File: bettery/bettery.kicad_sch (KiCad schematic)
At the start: 77 parts, among them Q1 WMB014N06LG4, Q2 WMB014N06LG4, Q3 SL2319A, Q4 MMBT3904, SW1 SW_Push, U1 L9961

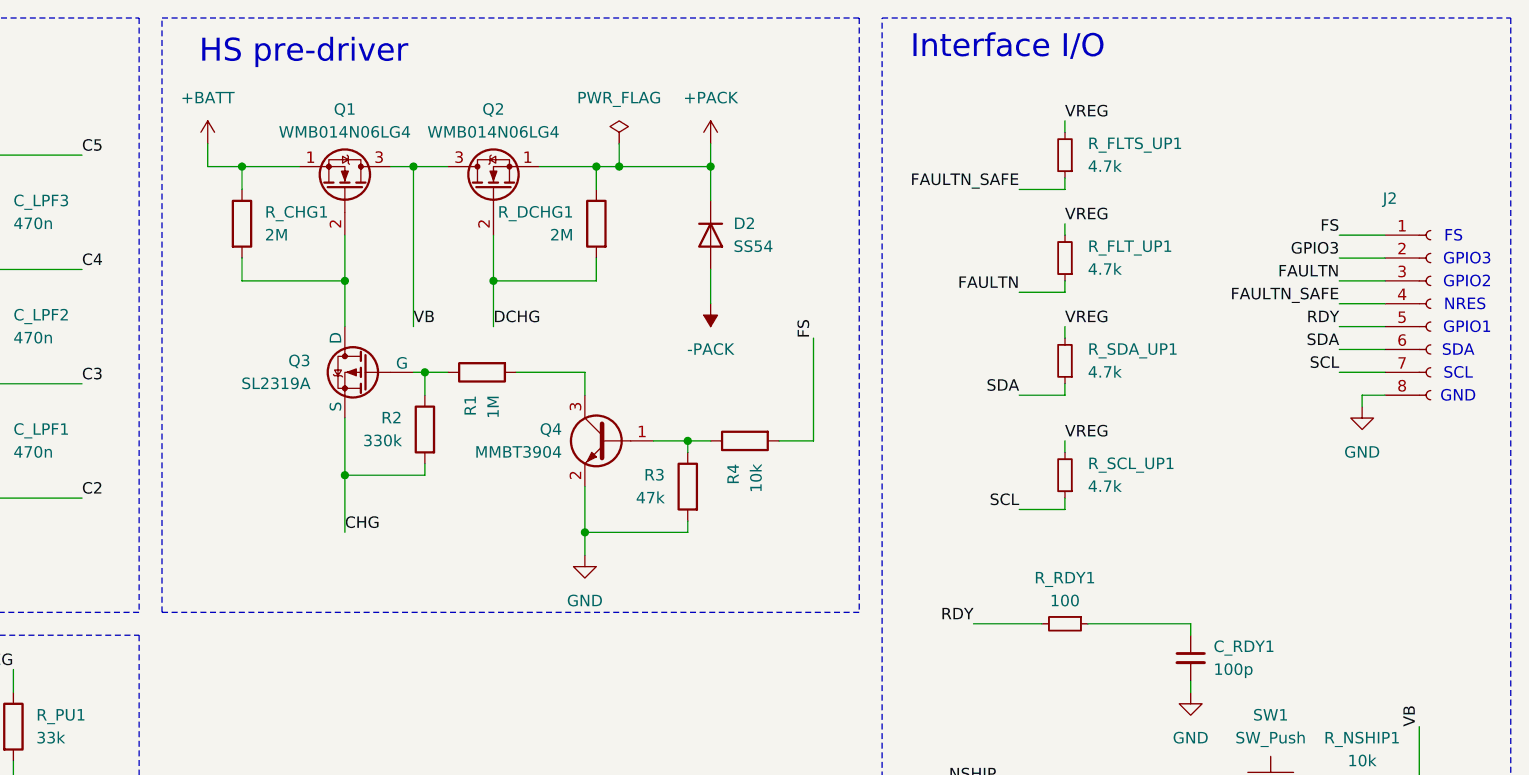
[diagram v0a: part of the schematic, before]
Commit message: remove fail-safe switch
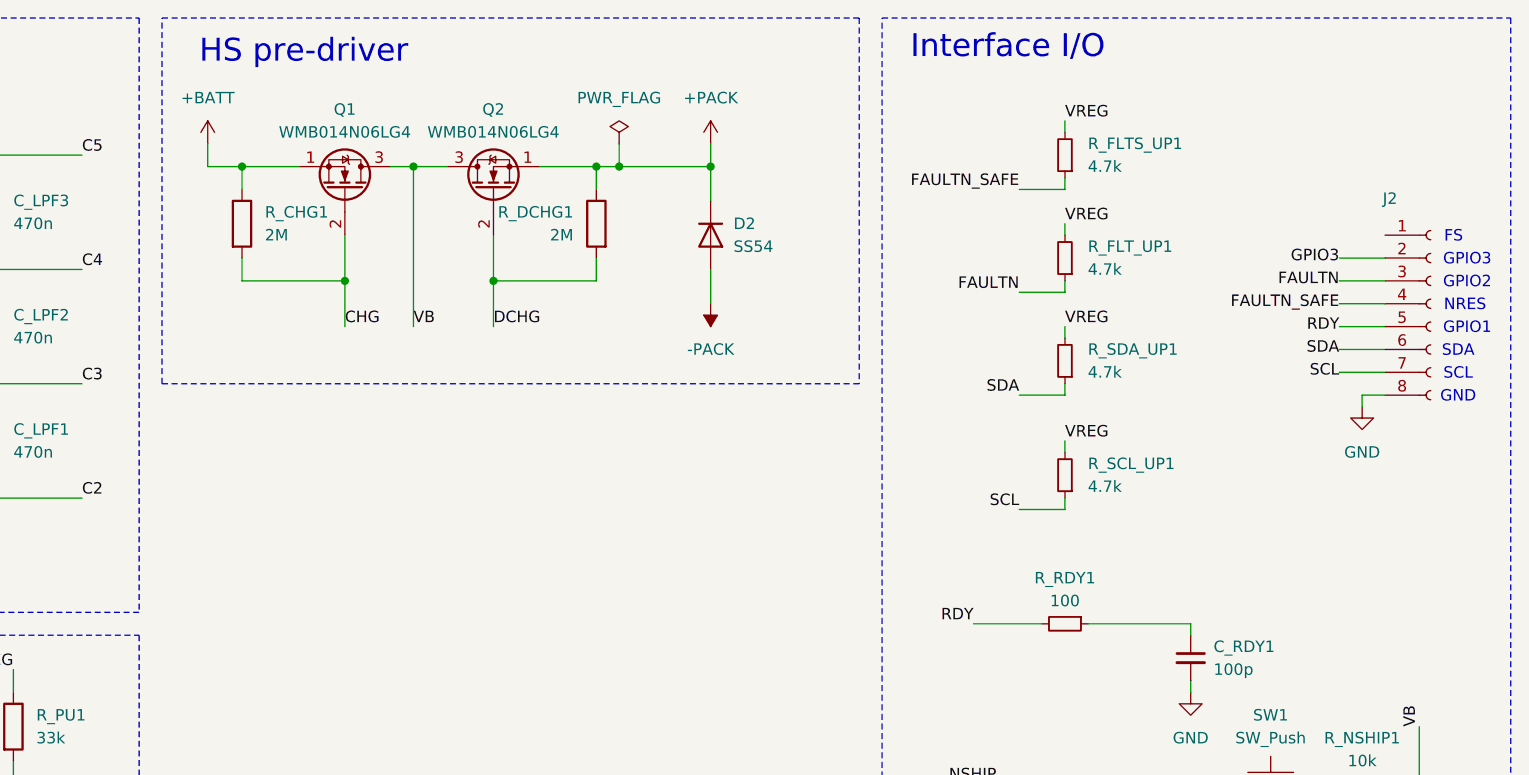
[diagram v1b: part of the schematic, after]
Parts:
- removed Q3: SL2319A, Package_TO_SOT_SMD:SOT-23_Handsoldering, symbol Simulation_SPICE:PMOS
- removed Q4: MMBT3904, Package_TO_SOT_SMD:SOT-23_Handsoldering, symbol Transistor_BJT:Q_NPN_BEC
- removed R1: 1M, Resistor_SMD:R_0603_1608Metric_Pad0.98x0.95mm_HandSolder, symbol Device:R
- removed R2: 330k, Resistor_SMD:R_0603_1608Metric_Pad0.98x0.95mm_HandSolder, symbol Device:R
- removed R3: 47k, Resistor_SMD:R_0603_1608Metric_Pad0.98x0.95mm_HandSolder, symbol Device:R
- removed R4: 10k, Resistor_SMD:R_0603_1608Metric_Pad0.98x0.95mm_HandSolder, symbol Device:R
- J_CHG1: footprint (none) -> Connector_BarrelJack:BarrelJack_GCT_DCJ200-10-A_Horizontal; Link (none) -> https://www.digikey.com/en/products/detail/tensility-intern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
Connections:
- net CHG: now also Q1.2 (G), R_CHG1.2
- net FS: no longer names the net of J2.1 (Pin_1)

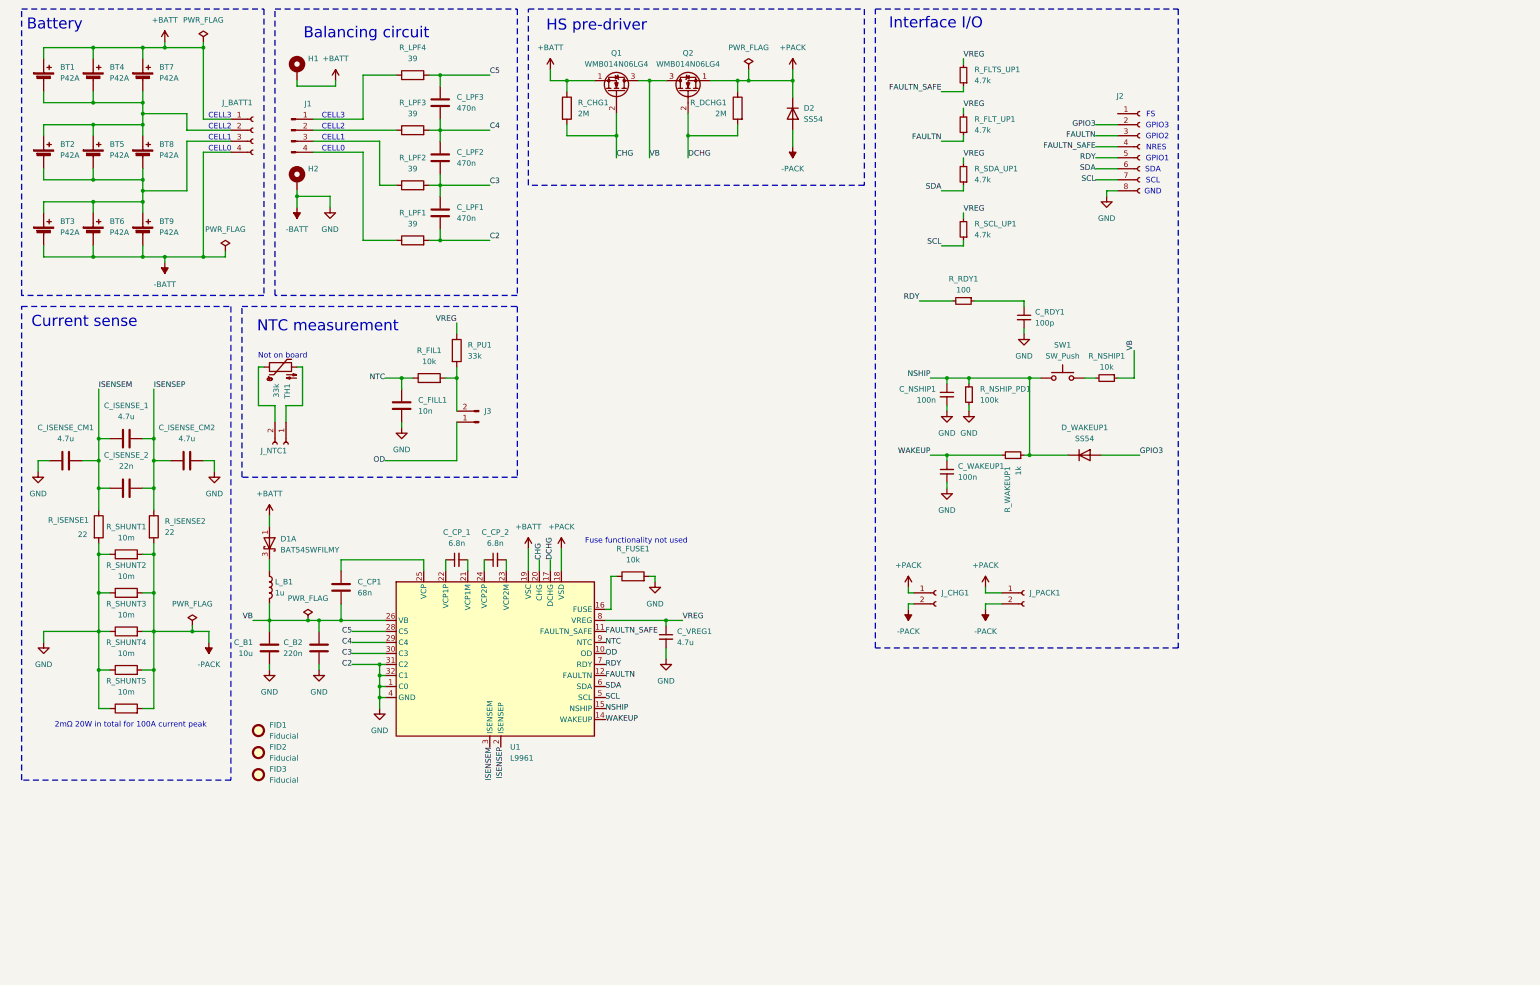
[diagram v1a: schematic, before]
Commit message: add mcu
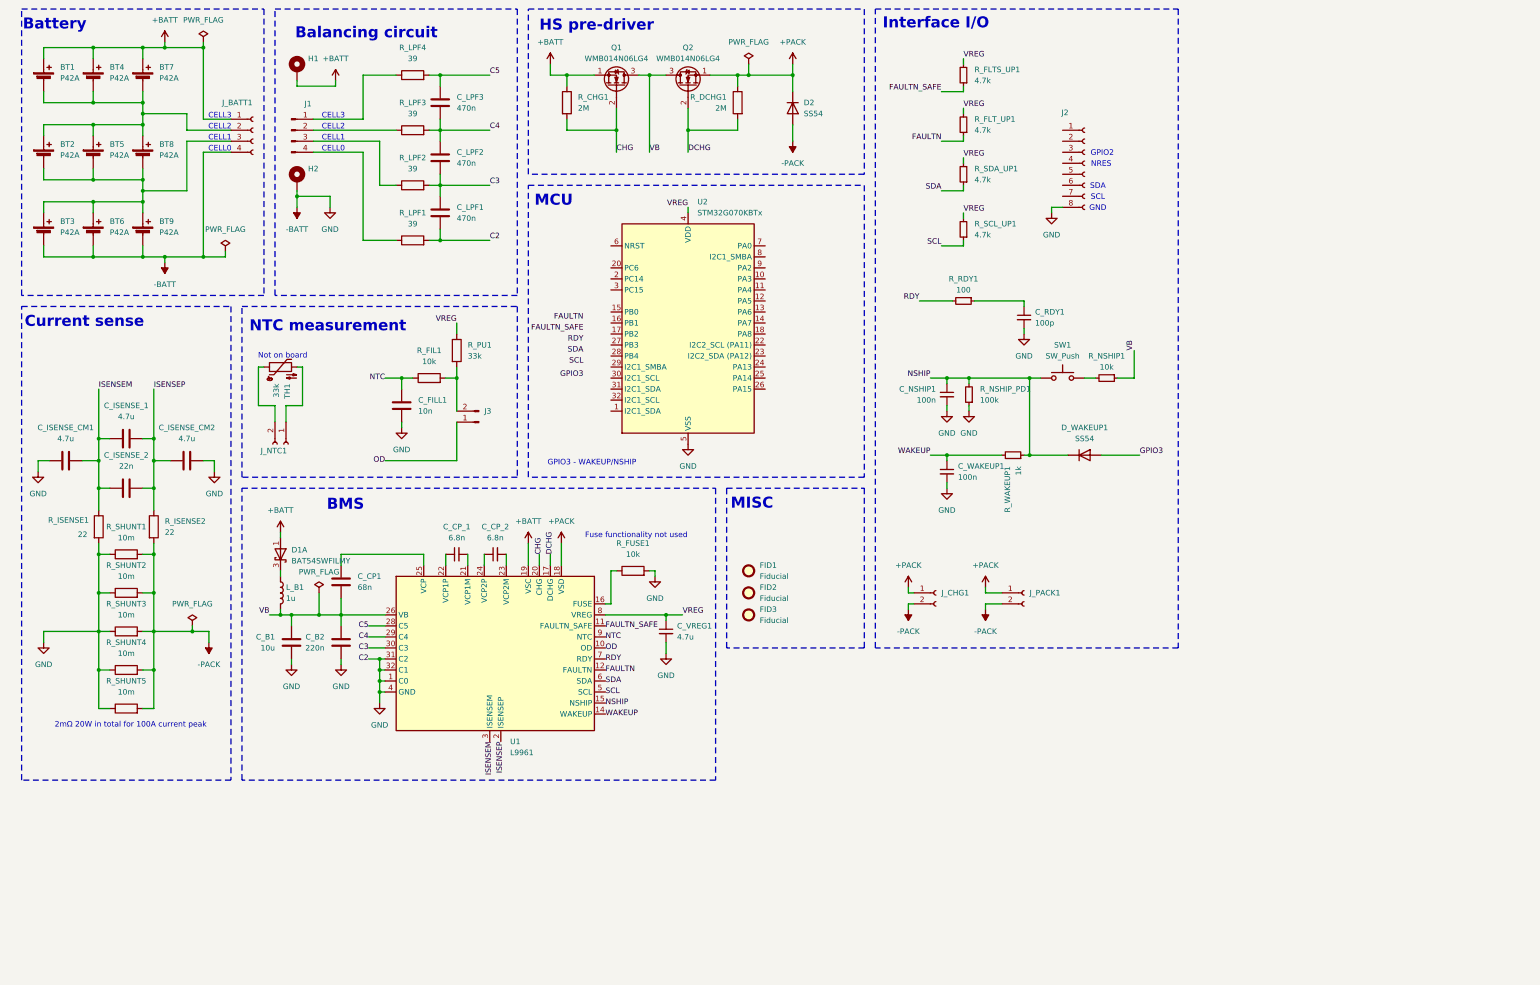
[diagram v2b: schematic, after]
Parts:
- added U2: STM32G070KBTx, Package_QFP:LQFP-32_7x7mm_P0.8mm, symbol MCU_ST_STM32G0:STM32G070KBTx
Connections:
- net -BATT: now also U2.5 (VSS)
- net FAULTN: no longer J2.3 (Pin_3)
- net FAULTN_SAFE: no longer J2.4 (Pin_4)
- net GPIO3: no longer J2.2 (Pin_2)
- net RDY: no longer J2.5 (Pin_5)
- net SCL: no longer J2.7 (Pin_7)
- net SDA: no longer J2.6 (Pin_6)
- net VREG: now also U2.4 (VDD)
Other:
- note added: "BMS"
- note added: "GPIO3 - WAKEUP/NSHIP"
- note added: "MCU"
- note added: "MISC"
- note removed: "FS"
- note removed: "GPIO1"
- note removed: "GPIO3"
- moved on the sheet: C_B1, C_B2, C_CP1, C_CP_1, C_CP_2, C_VREG1, D1A, D2, FID1, FID2, FID3, J2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

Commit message: complete routing
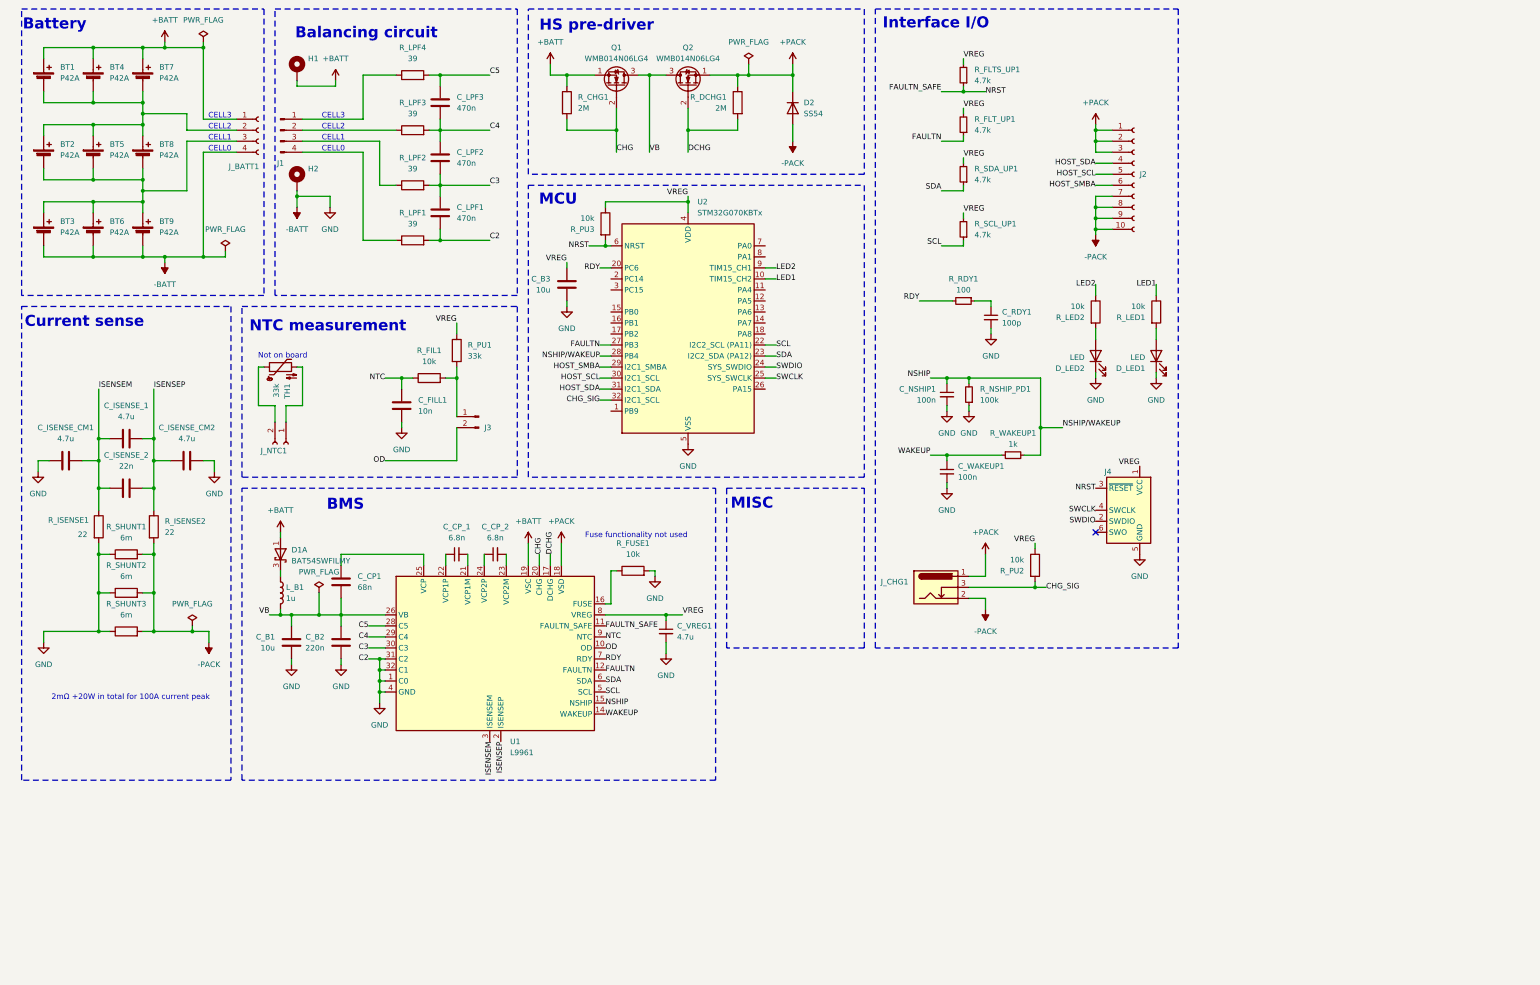
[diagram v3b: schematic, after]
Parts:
- removed D_WAKEUP1: SS54, Diode_SMD:D_SMA_Handsoldering, symbol Device:D
- removed FID1, FID2, FID3: Fiducial, Fiducial:Fiducial_1mm_Mask3mm, symbol Mechanical:Fiducial
- removed J2: ~, Connector_JST:JST_PH_B8B-PH-K_1x08_P2.00mm_Vertical, symbol Connector:Conn_01x08_Socket
- removed J_CHG1: ~, Connector_BarrelJack:BarrelJack_GCT_DCJ200-10-A_Horizontal, symbol Connector:Conn_01x02_Socket
- removed J_PACK1: ~, symbol Connector:Conn_01x02_Socket
- removed R_NSHIP1: 10k, Resistor_SMD:R_0603_1608Metric_Pad0.98x0.95mm_HandSolder, symbol Device:R_Small
- removed R_SHUNT4, R_SHUNT5: 10m, Resistor_SMD:R_2816_7142Metric_Pad3.20x4.45mm_HandSolder, symbol Device:R
- removed SW1: SW_Push, Button_Switch_THT:SW_PUSH_6mm, symbol Switch:SW_Push
- added C_B3: 10u, Capacitor_SMD:C_0603_1608Metric, symbol Device:C
- added D_LED1, D_LED2: LED, LED_SMD:LED_0603_1608Metric, symbol Device:LED
- added J2: Conn_01x10_Socket, bettery:1674231_SMD, symbol Connector:Conn_01x10_Socket
- added J4: Conn_ARM_SWD_TagConnect_TC2030, bettery:WR-WST-REDFIT-IDC-6pin, symbol Connector:Conn_ARM_SWD_TagConnect_TC2030
- added J_CHG1: Barrel_Jack_Switch, Connector_BarrelJack:BarrelJack_GCT_DCJ200-10-A_Horizontal, symbol Connector:Barrel_Jack_Switch
- added R_LED1, R_LED2, R_PU2, R_PU3: 10k, Resistor_SMD:R_0603_1608Metric, symbol Device:R
- C_B1, C_B2, C_CP1, C_CP_1, C_CP_2, C_FILL1, C_ISENSE_1, C_ISENSE_2, C_ISENSE_CM1, C_ISENSE_CM2, C_LPF1, C_LPF2, C_LPF3, C_NSHIP1, C_RDY1, C_VREG1, C_WAKEUP1: footprint Capacitor_SMD:C_0603_1608Metric_Pad1.08x0.95mm_HandSolder -> Capacitor_SMD:C_0603_1608Metric
- D1: footprint Package_TO_SOT_SMD:SOT-323_SC-70_Handsoldering -> Package_TO_SOT_SMD:SOT-323_SC-70
- H1, H2: footprint (none) -> Connector_Wire:SolderWirePad_1x01_SMD_5x10mm
- J1: footprint Connector_JST:JST_PH_B4B-PH-K_1x04_P2.00mm_Vertical -> Connector_JST:JST_PH_S4B-PH-K_1x04_P2.00mm_Horizontal
- J3: footprint Connector_JST:JST_PH_B2B-PH-K_1x02_P2.00mm_Vertical -> Connector_JST:JST_PH_S2B-PH-K_1x02_P2.00mm_Horizontal
- L_B1: footprint Inductor_SMD:L_0805_2012Metric_Pad1.05x1.20mm_HandSolder -> Inductor_SMD:L_0805_2012Metric
- R_CHG1, R_DCHG1, R_FIL1, R_FLTS_UP1, R_FLT_UP1, R_FUSE1, R_ISENSE1, R_ISENSE2, R_LPF1, R_LPF2, R_LPF3, R_LPF4, R_NSHIP_PD1, R_PU1, R_RDY1, R_SCL_UP1, R_SDA_UP1, R_WAKEUP1: footprint Resistor_SMD:R_0603_1608Metric_Pad0.98x0.95mm_HandSolder -> Resistor_SMD:R_0603_1608Metric
- R_SHUNT1, R_SHUNT2, R_SHUNT3: value 10m -> 6m; footprint Resistor_SMD:R_2816_7142Metric_Pad3.20x4.45mm_HandSolder -> bettery:R_Shunt_Vishay_WSHP2818; PN (none) -> WSHP28186L000FEA
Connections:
- net +PACK: now also J2.1 (Pin_1), J2.2 (Pin_2), J2.3 (Pin_3), J_CHG1.1
- net -BATT: now also C_B3.2, D_LED1.1 (K), D_LED2.1 (K), J4.5 (GND)
- net -PACK: now also J2.10 (Pin_10), J2.7 (Pin_7), J2.8 (Pin_8), J2.9 (Pin_9), J_CHG1.2
- net FAULTN: now also U2.27 (PB3)
- net FAULTN_SAFE: now also U2.6 (NRST), J4.3 (~{RESET}), R_PU3.2
- net NSHIP: now also R_WAKEUP1.2, U2.28 (PB4); no longer R_WAKEUP1.1
- net OD: now also J3.2 (Pin_2); no longer J3.1 (Pin_1)
- net RDY: now also U2.20 (PC6)
- net SCL: now also U2.22 (PA9/PA11)
- net SDA: now also U2.23 (PA10/PA12)
- net VREG: now also C_B3.1, J4.1 (VCC), R_PU2.1, R_PU3.1
- net WAKEUP: now also R_WAKEUP1.1; no longer R_WAKEUP1.2
- net at R_FIL1.2, R_PU1.2: now also J3.1 (Pin_1); no longer J3.2 (Pin_2)
- net LED1: now reaches U2.10 (PA3)
- net LED1: now also R_LED1.1
- net SWDIO: now reaches U2.24 (PA13)
- net SWDIO: now also J4.2 (SWDIO)
- net SWCLK: now reaches U2.25 (PA14)
- net SWCLK: now also J4.4 (SWCLK)
- net HOST_SMBA: now reaches U2.29 (PB5)
- net HOST_SMBA: now also J2.6 (Pin_6)
- net HOST_SCL: now reaches U2.30 (PB6)
- net HOST_SCL: now also J2.5 (Pin_5)
- net HOST_SDA: now reaches U2.31 (PB7)
- net HOST_SDA: now also J2.4 (Pin_4)
- net CHG_SIG: now reaches U2.32 (PB8)
- net CHG_SIG: now also J_CHG1.3, R_PU2.2
- net LED2: now reaches U2.9 (PA2)
- net LED2: now also R_LED2.1
- new net: D_LED1.2 (A), R_LED1.2
- new net: D_LED2.2 (A), R_LED2.2
- no-connect marks 0 -> 1
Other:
- note added: "2mΩ +20W in total for 100A current peak"
- note removed: "2mΩ 20W in total for 100A current peak"
- note removed: "GND"
- note removed: "GPIO2"
- note removed: "GPIO3 - WAKEUP/NSHIP"
- note removed: "NRES"
- note removed: "SCL"
- note removed: "SDA"
- moved on the sheet: C_RDY1, J1, J3, J_BATT1, R_WAKEUP1
